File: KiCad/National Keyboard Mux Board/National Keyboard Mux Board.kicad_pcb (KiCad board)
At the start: 2 copper layers, 80 x 37.5 mm, 51 parts, among them J1 Conn_01x01_Female, J10 Conn_01x01_Female, J11 Conn_01x01_Female, J12 Conn_01x01_Female, J13 Conn_01x01_Female, J14 Conn_01x01_Female, J15 Conn_01x01_Female, J16 Conn_01x01_Female, J17 Conn_01x01_Female, J18 Conn_01x01_Female, J19 Conn_02x08_Odd_Even, J2 Conn_01x01_Female, J3 Conn_01x01_Female, J4 Conn_01x01_Female, J5 Conn_01x01_Female, J6 Conn_01x01_Female, J7 Conn_01x01_Female, J8 Conn_01x01_Female, J9 Conn_01x01_Female

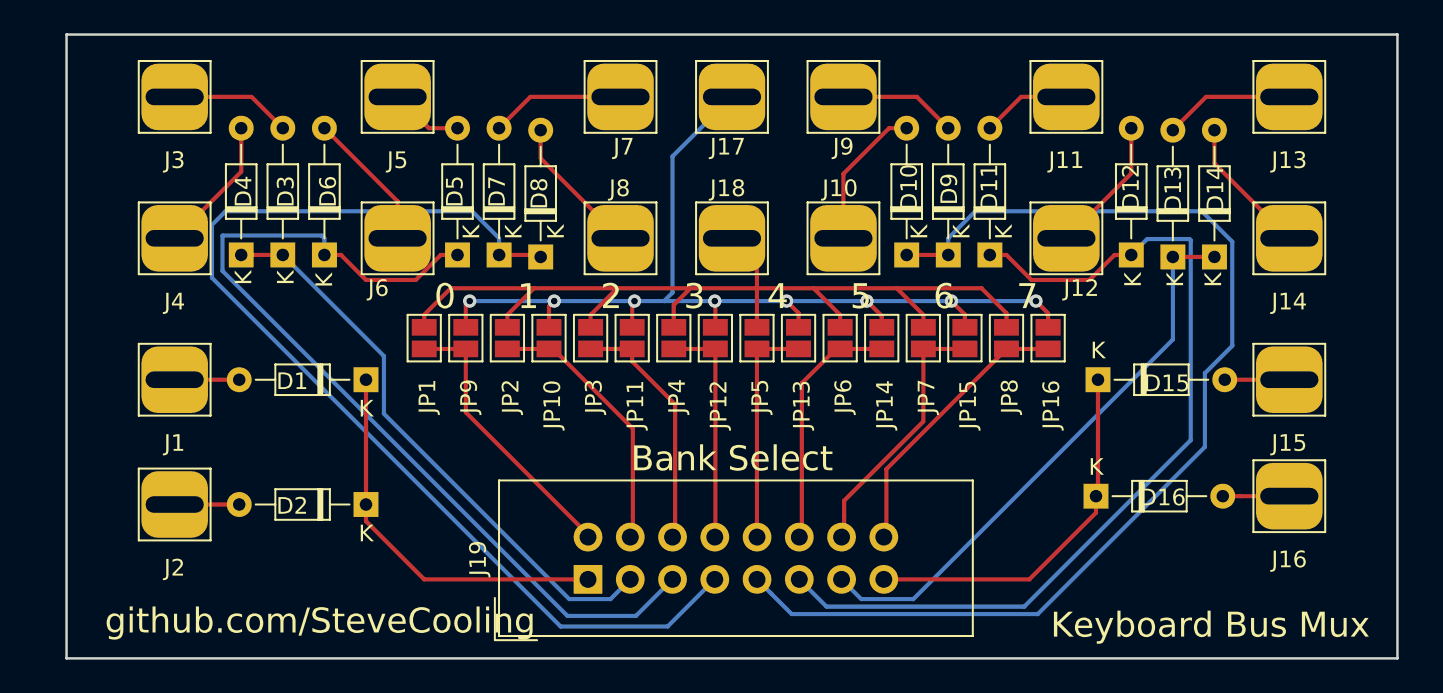
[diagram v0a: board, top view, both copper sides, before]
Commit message: Swithed to dual SMT diodes and made schematic prettier
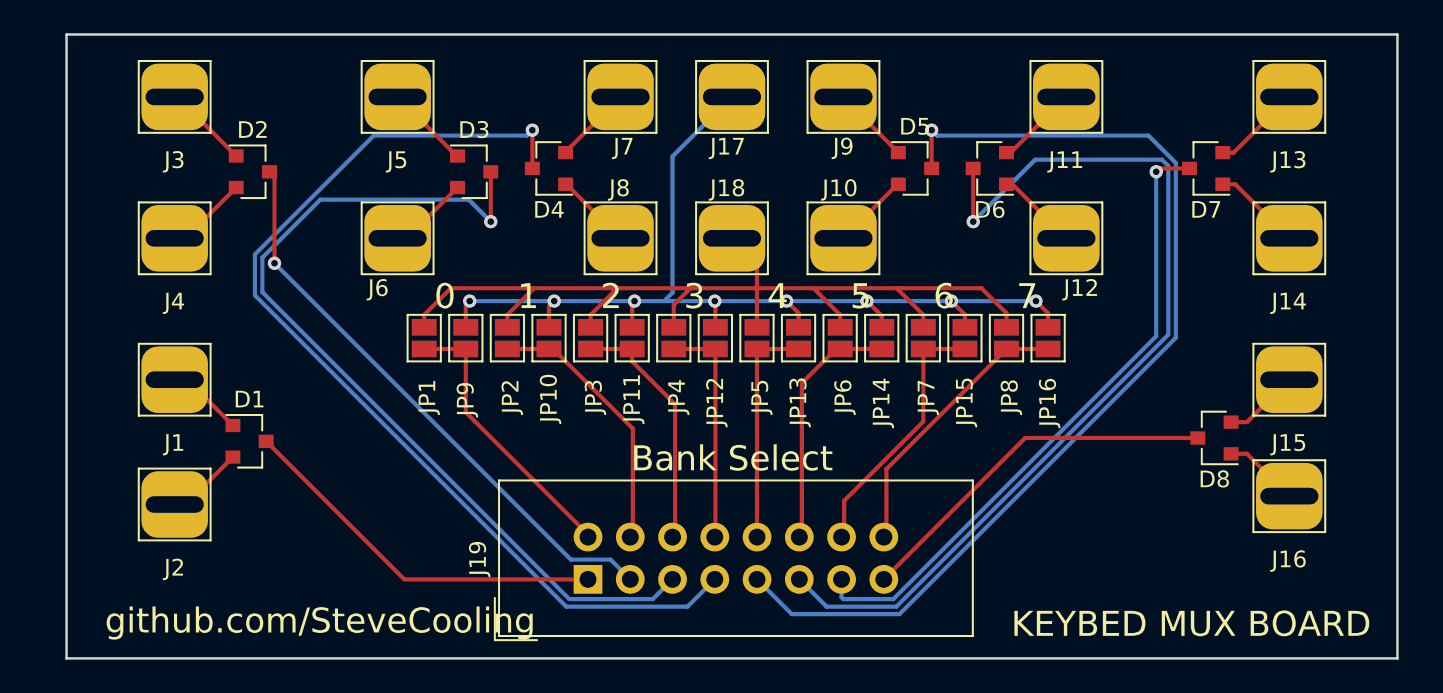
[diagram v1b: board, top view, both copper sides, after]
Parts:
- removed D10, D11, D12, D13, D14, D15, D16, D9: D, Diode_THT:D_DO-34_SOD68_P7.62mm_Horizontal
- D1: value 1N4148 -> BAV74LT1G; footprint Diode_THT:D_DO-34_SOD68_P7.62mm_Horizontal -> Package_TO_SOT_SMD:SOT-23
- D2, D3, D4, D5, D6, D7, D8: value D -> BAV74LT1G; footprint Diode_THT:D_DO-34_SOD68_P7.62mm_Horizontal -> Package_TO_SOT_SMD:SOT-23
- moved D7 42.8 mm to (138.5, 72.8), turned to 180 degrees
- moved D8 41.9 mm to (139.0, 89.0), turned to 180 degrees
- moved D6 40.3 mm to (125.5, 72.8), turned to 180 degrees
- moved D5 28.0 mm to (121.0, 72.8), turned to 0 degrees
- moved D2 21.1 mm to (81.2, 73.0), turned to 0 degrees
- moved D4 19.2 mm to (99.0, 72.8), turned to 180 degrees
- moved D3 12.5 mm to (94.5, 73.0), turned to 0 degrees
- moved D1 7.92 mm to (81.0, 89.2), turned to 0 degrees
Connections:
- net Net-(J17-Pad1) renamed /COMMON_UPPER
- net Net-(J18-Pad1) renamed /COMMON_LOWER
- net Net-(J19-Pad10) renamed /GROUP5
- net Net-(J19-Pad12) renamed /GROUP6
- net Net-(J19-Pad14) renamed /GROUP7
- net Net-(J19-Pad16) renamed /GROUP8
- net Net-(J19-Pad2) renamed /GROUP1
- net Net-(J19-Pad4) renamed /GROUP2
- net Net-(J19-Pad6) renamed /GROUP3
- net Net-(J19-Pad8) renamed /GROUP4
- D2 pad 1: Net-(D1-Pad1) -> Net-(D2-Pad1)
- D4 pad 1: Net-(D3-Pad1) -> Net-(D4-Pad1)
- D6 pad 1: Net-(D5-Pad1) -> Net-(D6-Pad1)
- D8 pad 1: Net-(D7-Pad1) -> Net-(D8-Pad1)
- J1 pad 1: Net-(D1-Pad2) -> Net-(D1-Pad1)
- J10 pad 1: Net-(D10-Pad2) -> Net-(D5-Pad2)
- J11 pad 1: Net-(D11-Pad2) -> Net-(D6-Pad2)
- J12 pad 1: Net-(D12-Pad2) -> Net-(D6-Pad1)
- J13 pad 1: Net-(D13-Pad2) -> Net-(D7-Pad2)
- J14 pad 1: Net-(D14-Pad2) -> Net-(D7-Pad1)
- J15 pad 1: Net-(D15-Pad2) -> Net-(D8-Pad2)
- J16 pad 1: Net-(D16-Pad2) -> Net-(D8-Pad1)
- J19 pad 1: Net-(D1-Pad1) -> /KEY1
- J19 pad 11: Net-(D11-Pad1) -> /KEY6
- J19 pad 13: Net-(D13-Pad1) -> /KEY7
- J19 pad 15: Net-(D15-Pad1) -> /KEY8
- J19 pad 3: Net-(D3-Pad1) -> /KEY2
- J19 pad 5: Net-(D5-Pad1) -> /KEY3
- J19 pad 7: Net-(D7-Pad1) -> /KEY4
- J19 pad 9: Net-(D10-Pad1) -> /KEY5
- J2 pad 1: Net-(D2-Pad2) -> Net-(D1-Pad2)
- J3 pad 1: Net-(D3-Pad2) -> Net-(D2-Pad1)
- J4 pad 1: Net-(D4-Pad2) -> Net-(D2-Pad2)
- J5 pad 1: Net-(D5-Pad2) -> Net-(D3-Pad1)
- J6 pad 1: Net-(D6-Pad2) -> Net-(D3-Pad2)
- J7 pad 1: Net-(D7-Pad2) -> Net-(D4-Pad2)
- J8 pad 1: Net-(D8-Pad2) -> Net-(D4-Pad1)
- J9 pad 1: Net-(D9-Pad2) -> Net-(D5-Pad1)
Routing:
- net Net-(D10-Pad1): track 67.0 -> 0.00 mm
- net /KEY5: track 0.00 -> 61.2 mm, vias 0 -> 1
- net /KEY4: track 0.00 -> 60.6 mm, vias 0 -> 1
- net Net-(D7-Pad1): track 65.1 -> 5.35 mm
- net /KEY6: track 0.00 -> 56.4 mm, vias 0 -> 1
- net Net-(D11-Pad1): track 54.1 -> 0.00 mm
- net /KEY3: track 0.00 -> 53.6 mm, vias 0 -> 1
- net Net-(D5-Pad1): track 55.1 -> 4.72 mm
- net /KEY7: track 0.00 -> 38.6 mm, vias 0 -> 1
- net /KEY2: track 0.00 -> 34.9 mm, vias 0 -> 1
- net Net-(D13-Pad1): track 34.3 -> 0.00 mm
- net Net-(D3-Pad1): track 34.5 -> 5.07 mm
- net /KEY1: track 0.00 -> 22.8 mm
- net /KEY8: track 0.00 -> 22.4 mm
- net Net-(D15-Pad1): track 22.3 -> 0.00 mm
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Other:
- board text added: "KEYBED MUX BOARD"
- board text removed: "Keyboard Bus Mux"

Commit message: production files
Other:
- board text added: "KEYBED MUX BOARD rev. 1"
- board text added: "bzzt.no"
- board text removed: "KEYBED MUX BOARD"
- board text removed: "github.com/SteveCooling"

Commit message: more work towards production
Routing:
- added copper zone on B.Cu, net (none)
- added copper zone on F.Cu, net (none)
